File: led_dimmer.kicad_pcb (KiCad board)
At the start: 2 copper layers, 23.5 x 25.1 mm, 13 parts, among them P1 CONN_2, P2 CONN_2, Q1 MOSFET_N, U1 555

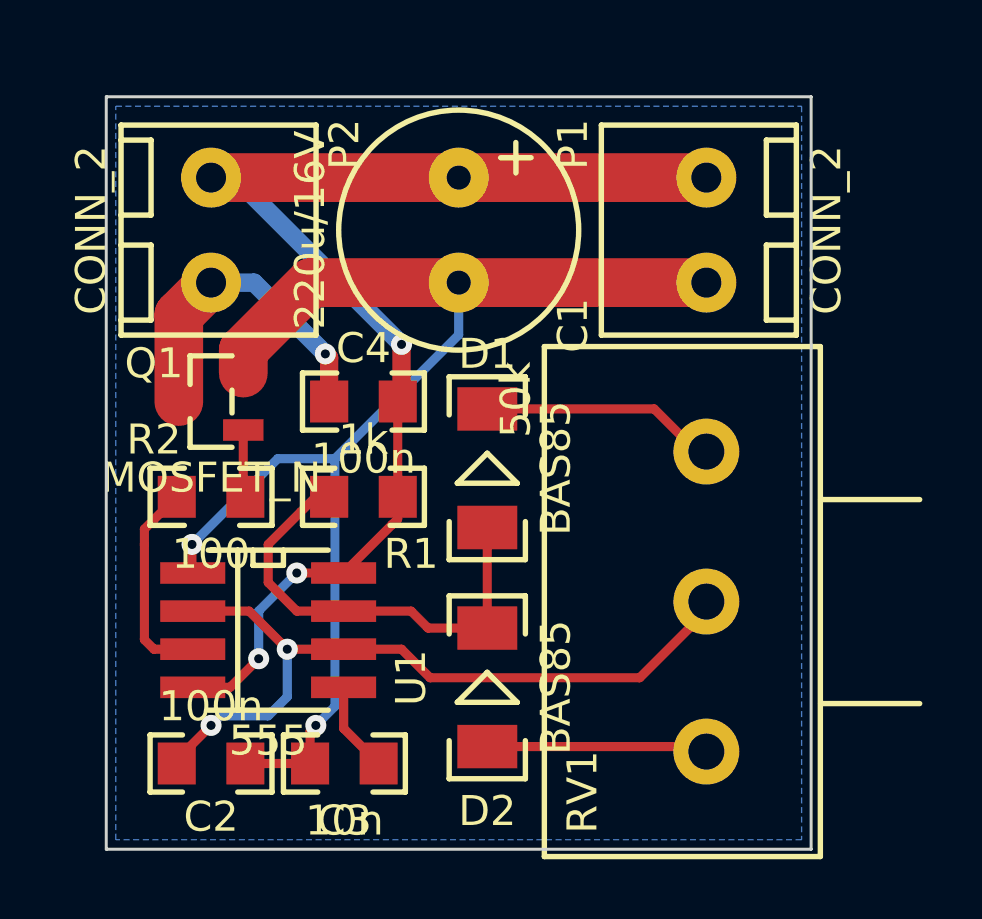
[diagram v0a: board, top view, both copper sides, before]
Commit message: larger vias, silk screen update
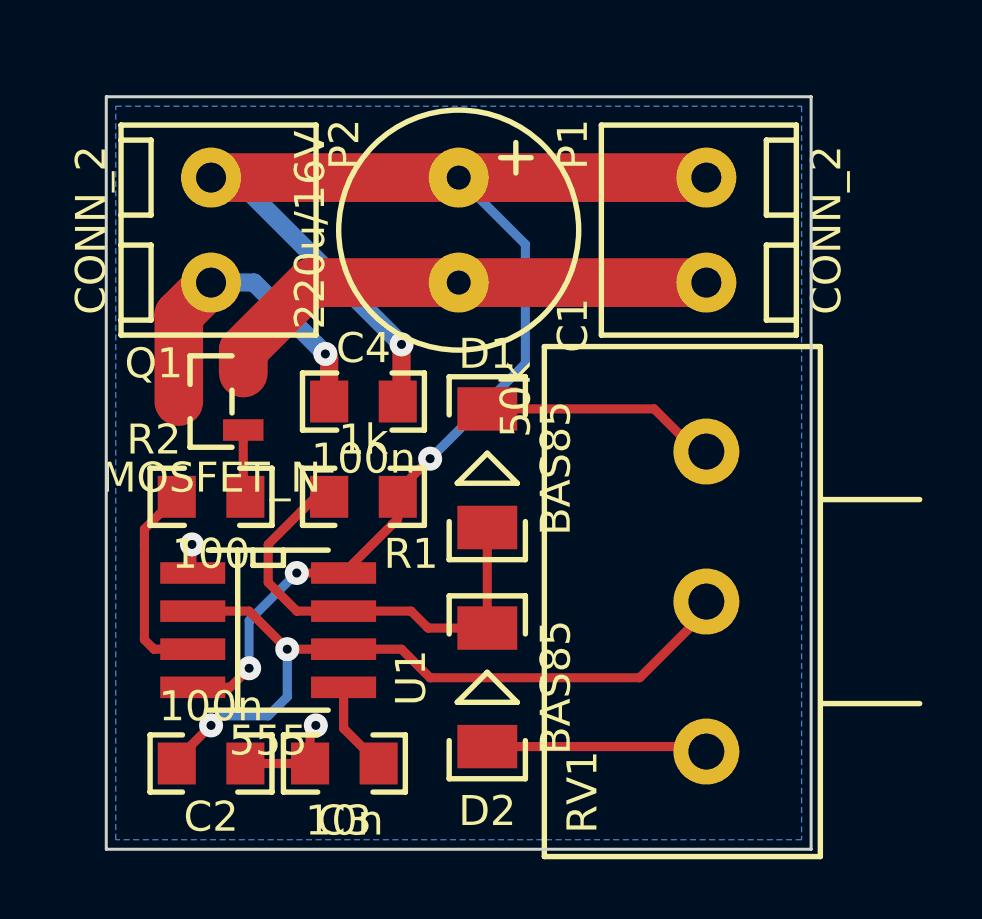
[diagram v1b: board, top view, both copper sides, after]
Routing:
- net GND: track 44.3 -> 21.8 mm
- net VCC: track 41.1 -> 51.3 mm, vias 3 -> 4
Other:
- net class Default: clearance 0.2794 -> 0.3048; via_dia 0.7 -> 0.8
- rule trace_clearance: 0.2794 -> 0.3048
- rule via_min_size: 0.7 -> 0.8
- board text added: "LED"
- board text added: "LED dimmer"
- board text added: "PWR"
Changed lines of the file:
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@@
     (links 24)
     (no_connects 0)
-    (area 148.912029 97.965 180.201401 124.121901)
+    (area 148.886629 97.965 180.226801 124.147301)
     (thickness 1.6)
-    (drawings 8)
+    (drawings 11)
     (tracks 80)
     (zones 0)
@@
     (18 B.Paste user)
     (19 F.Paste user)
-    (20 B.SilkS user)
+    (20 B.SilkS user hide)
     (21 F.SilkS user)
     (22 B.Mask user)
@@
     (user_trace_width 0.6096)
     (user_trace_width 1.6256)
-    (trace_clearance 0.2794)
+    (trace_clearance 0.3048)
     (zone_clearance 0.2794)
     (zone_45_only no)
@@
     (segment_width 0.2)
     (edge_width 0.1)
-    (via_size 0.7)
+    (via_size 0.8)
     (via_drill 0.3)
-    (via_min_size 0.7)
+    (via_min_size 0.8)
     (via_min_drill 0.3)
     (uvia_size 0.508)
@@
   (net 10 VCC)
   (net_class Default "This is the default net class."
-    (clearance 0.2794)
+    (clearance 0.3048)
     (trace_width 0.3048)
-    (via_dia 0.7)
+    (via_dia 0.8)
     (via_drill 0.3)
     (uvia_dia 0.508)
@@
     )
   )
+  (gr_text PWR (at 172.72 107.315) (layer B.SilkS)
+    (effects (font (size 1.5 1.5) (thickness 0.3)) (justify mirror))
+  )
+  (gr_text LED (at 156.21 107.315) (layer B.SilkS)
+    (effects (font (size 1.5 1.5) (thickness 0.3)) (justify mirror))
+  )
+  (gr_text "LED\ndimmer" (at 163.83 116.205 90) (layer B.SilkS)
+    (effects (font (size 2 2) (thickness 0.3)) (justify mirror))
+  )
   (gr_text - (at 169.545 104.4575) (layer B.SilkS)
     (effects (font (size 3 3) (thickness 0.6)) (justify mirror))
@@
   (gr_line (start 176.2125 98.425) (end 152.7175 98.425) (angle 90) (layer Edge.Cuts) (width 0.1))
   (gr_line (start 152.7175 123.5075) (end 176.2125 123.5075) (angle 90) (layer Edge.Cuts) (width 0.1))
+  (segment (start 164.465 104.62) (end 164.465 104.775) (width 0.3048) (layer B.Cu) (net 1))
   (segment (start 155.6 114.3) (end 155.575 114.275) (width 0.3048) (layer F.Cu) (net 1))
-  (segment (start 158.4325 110.49) (end 160.3375 110.49) (width 0.3048) (layer B.Cu) (net 1))
-  (segment (start 155.575 113.3475) (end 158.4325 110.49) (width 0.3048) (layer B.Cu) (net 1))
-  (via (at 155.575 113.3475) (size 0.7) (layers F.Cu B.Cu) (net 1))
   (segment (start 155.575 114.275) (end 155.575 113.3475) (width 0.3048) (layer F.Cu) (net 1))
-  (segment (start 160.3375 110.49) (end 164.465 106.3625) (width 0.3048) (layer B.Cu) (net 1))
+  (via (at 155.575 113.3475) (size 0.8) (layers F.Cu B.Cu) (net 1))
   (segment (start 159.512 119.5705) (end 159.7025 119.38) (width 0.3048) (layer F.Cu) (net 1))
-  (via (at 159.7025 119.38) (size 0.7) (layers F.Cu B.Cu) (net 1))
-  (segment (start 159.7025 119.38) (end 160.3375 118.745) (width 0.3048) (layer B.Cu) (net 1))
-  (segment (start 160.3375 118.745) (end 160.3375 110.49) (width 0.3048) (layer B.Cu) (net 1))
   (segment (start 159.512 120.65) (end 159.512 119.5705) (width 0.3048) (layer F.Cu) (net 1) (status 10))
-  (segment (start 164.465 106.3625) (end 164.465 104.62) (width 0.3048) (layer B.Cu) (net 1))
+  (via (at 159.7025 119.38) (size 0.8) (layers F.Cu B.Cu) (net 1))
   (segment (start 157.285 107.635) (end 157.285 106.875) (width 1.6256) (layer F.Cu) (net 1) (status 10))
   (segment (start 157.285 106.875) (end 159.54 104.62) (width 1.6256) (layer F.Cu) (net 1))
@@
   (segment (start 162.56 116.84) (end 163.5125 117.7925) (width 0.3048) (layer F.Cu) (net 2))
   (segment (start 155.067 120.65) (end 155.067 120.523) (width 0.3048) (layer F.Cu) (net 2) (status 30))
-  (via (at 158.75 116.84) (size 0.7) (layers F.Cu B.Cu) (net 2))
+  (via (at 158.75 116.84) (size 0.8) (layers F.Cu B.Cu) (net 2))
   (segment (start 158.75 118.4275) (end 158.75 116.84) (width 0.3048) (layer B.Cu) (net 2))
   (segment (start 158.115 119.0625) (end 158.75 118.4275) (width 0.3048) (layer B.Cu) (net 2))
   (segment (start 156.5275 119.0625) (end 158.115 119.0625) (width 0.3048) (layer B.Cu) (net 2))
   (segment (start 156.21 119.38) (end 156.5275 119.0625) (width 0.3048) (layer B.Cu) (net 2))
-  (via (at 156.21 119.38) (size 0.7) (layers F.Cu B.Cu) (net 2))
+  (via (at 156.21 119.38) (size 0.8) (layers F.Cu B.Cu) (net 2))
   (segment (start 155.067 120.523) (end 156.21 119.38) (width 0.3048) (layer F.Cu) (net 2) (status 10))
   (segment (start 160.63 116.84) (end 158.75 116.84) (width 0.3048) (layer F.Cu) (net 2) (status 10))
@@
   (segment (start 157.6425 104.62) (end 156.21 104.62) (width 0.6096) (layer B.Cu) (net 4) (status 20))
   (segment (start 160.02 106.9975) (end 157.6425 104.62) (width 0.6096) (layer B.Cu) (net 4))
-  (via (at 160.02 106.9975) (size 0.7) (layers F.Cu B.Cu) (net 4))
+  (via (at 160.02 106.9975) (size 0.8) (layers F.Cu B.Cu) (net 4))
   (segment (start 160.147 107.1245) (end 160.02 106.9975) (width 0.6096) (layer F.Cu) (net 4))
   (segment (start 155.135 108.585) (end 155.135 105.695) (width 1.6256) (layer F.Cu) (net 4) (status 10))
@@
   (segment (start 153.9875 116.5225) (end 154.305 116.84) (width 0.3048) (layer F.Cu) (net 9))
   (segment (start 153.9875 112.8395) (end 153.9875 113.3475) (width 0.3048) (layer F.Cu) (net 9))
-  (segment (start 162.433 108.585) (end 162.433 111.76) (width 0.3048) (layer F.Cu) (net 10))
+  (segment (start 162.433 111.76) (end 162.433 111.5695) (width 0.3048) (layer F.Cu) (net 10))
+  (segment (start 166.6875 103.3425) (end 164.465 101.12) (width 0.3048) (layer B.Cu) (net 10))
+  (segment (start 166.6875 107.315) (end 166.6875 103.3425) (width 0.3048) (layer B.Cu) (net 10))
+  (segment (start 163.5125 110.49) (end 166.6875 107.315) (width 0.3048) (layer B.Cu) (net 10))
+  (via (at 163.5125 110.49) (size 0.8) (layers F.Cu B.Cu) (net 10))
+  (segment (start 162.433 111.5695) (end 163.5125 110.49) (width 0.3048) (layer F.Cu) (net 10))
   (segment (start 162.433 111.76) (end 162.433 112.497) (width 0.3048) (layer F.Cu) (net 10))
   (segment (start 162.2425 112.6875) (end 160.63 114.3) (width 0.3048) (layer F.Cu) (net 10) (status 20))
@@
   (segment (start 160.63 114.3) (end 159.0675 114.3) (width 0.3048) (layer F.Cu) (net 10) (status 10))
   (segment (start 156.845 118.11) (end 155.6 118.11) (width 0.3048) (layer F.Cu) (net 10) (status 20))
-  (segment (start 157.7975 117.1575) (end 156.845 118.11) (width 0.3048) (layer F.Cu) (net 10))
-  (via (at 157.7975 117.1575) (size 0.7) (layers F.Cu B.Cu) (net 10))
-  (segment (start 157.7975 115.57) (end 157.7975 117.1575) (width 0.3048) (layer B.Cu) (net 10))
-  (segment (start 159.0675 114.3) (end 157.7975 115.57) (width 0.3048) (layer B.Cu) (net 10))
-  (via (at 159.0675 114.3) (size 0.7) (layers F.Cu B.Cu) (net 10))
+  (segment (start 157.48 117.475) (end 156.845 118.11) (width 0.3048) (layer F.Cu) (net 10))
+  (via (at 157.48 117.475) (size 0.8) (layers F.Cu B.Cu) (net 10))
+  (segment (start 157.48 115.8875) (end 157.48 117.475) (width 0.3048) (layer B.Cu) (net 10))
+  (segment (start 159.0675 114.3) (end 157.48 115.8875) (width 0.3048) (layer B.Cu) (net 10))
+  (via (at 159.0675 114.3) (size 0.8) (layers F.Cu B.Cu) (net 10))
   (segment (start 162.433 108.585) (end 162.56 108.458) (width 0.6096) (layer F.Cu) (net 10) (status 30))
   (segment (start 162.56 108.458) (end 162.56 106.68) (width 0.6096) (layer F.Cu) (net 10) (status 10))
   (segment (start 157 101.12) (end 156.21 101.12) (width 0.6096) (layer B.Cu) (net 10) (status 30))
   (segment (start 162.56 106.68) (end 157 101.12) (width 0.6096) (layer B.Cu) (net 10) (status 20))
-  (via (at 162.56 106.68) (size 0.7) (layers F.Cu B.Cu) (net 10))
+  (via (at 162.56 106.68) (size 0.8) (layers F.Cu B.Cu) (net 10))
   (segment (start 156.21 101.12) (end 164.465 101.12) (width 1.6256) (layer F.Cu) (net 10) (status 30))
   (segment (start 164.465 101.12) (end 172.72 101.12) (width 1.6256) (layer F.Cu) (net 10) (status 30))

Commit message: removed redundant vias
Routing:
- net Net-(C2-Pad2): track 25.2 -> 24.7 mm, vias 2 -> 0
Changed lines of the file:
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@@
     (thickness 1.6)
     (drawings 11)
-    (tracks 80)
+    (tracks 74)
     (zones 0)
     (modules 13)
@@
   (gr_line (start 176.2125 98.425) (end 152.7175 98.425) (angle 90) (layer Edge.Cuts) (width 0.1))
   (gr_line (start 152.7175 123.5075) (end 176.2125 123.5075) (angle 90) (layer Edge.Cuts) (width 0.1))
-  (segment (start 164.465 104.62) (end 164.465 104.775) (width 0.3048) (layer B.Cu) (net 1))
-  (segment (start 155.6 114.3) (end 155.575 114.275) (width 0.3048) (layer F.Cu) (net 1))
-  (segment (start 155.575 114.275) (end 155.575 113.3475) (width 0.3048) (layer F.Cu) (net 1))
+  (segment (start 164.465 104.62) (end 164.465 104.775) (width 0.3048) (layer B.Cu) (net 1) (status 30))
+  (segment (start 155.6 114.3) (end 155.575 114.275) (width 0.3048) (layer F.Cu) (net 1) (status 30))
+  (segment (start 155.575 114.275) (end 155.575 113.3475) (width 0.3048) (layer F.Cu) (net 1) (status 10))
   (via (at 155.575 113.3475) (size 0.8) (layers F.Cu B.Cu) (net 1))
   (segment (start 159.512 119.5705) (end 159.7025 119.38) (width 0.3048) (layer F.Cu) (net 1))
@@
   (segment (start 164.465 104.62) (end 172.72 104.62) (width 1.6256) (layer F.Cu) (net 1) (status 30))
   (segment (start 157.353 120.65) (end 159.512 120.65) (width 0.3048) (layer F.Cu) (net 1) (status 30))
-  (segment (start 160.63 116.84) (end 162.56 116.84) (width 0.3048) (layer F.Cu) (net 2))
-  (segment (start 170.4975 117.7925) (end 172.72 115.57) (width 0.3048) (layer F.Cu) (net 2))
+  (segment (start 158.75 116.84) (end 158.75 117.475) (width 0.3048) (layer F.Cu) (net 2))
+  (segment (start 155.067 120.523) (end 156.21 119.38) (width 0.3048) (layer F.Cu) (net 2) (status 10))
+  (segment (start 155.067 120.523) (end 155.067 120.65) (width 0.3048) (layer F.Cu) (net 2) (status 30))
+  (segment (start 156.845 119.38) (end 156.21 119.38) (width 0.3048) (layer F.Cu) (net 2))
+  (segment (start 158.75 117.475) (end 156.845 119.38) (width 0.3048) (layer F.Cu) (net 2))
+  (segment (start 160.63 116.84) (end 162.56 116.84) (width 0.3048) (layer F.Cu) (net 2) (status 10))
+  (segment (start 170.4975 117.7925) (end 172.72 115.57) (width 0.3048) (layer F.Cu) (net 2) (status 20))
   (segment (start 163.5125 117.7925) (end 170.4975 117.7925) (width 0.3048) (layer F.Cu) (net 2))
   (segment (start 162.56 116.84) (end 163.5125 117.7925) (width 0.3048) (layer F.Cu) (net 2))
-  (segment (start 155.067 120.65) (end 155.067 120.523) (width 0.3048) (layer F.Cu) (net 2) (status 30))
-  (via (at 158.75 116.84) (size 0.8) (layers F.Cu B.Cu) (net 2))
-  (segment (start 158.75 118.4275) (end 158.75 116.84) (width 0.3048) (layer B.Cu) (net 2))
-  (segment (start 158.115 119.0625) (end 158.75 118.4275) (width 0.3048) (layer B.Cu) (net 2))
-  (segment (start 156.5275 119.0625) (end 158.115 119.0625) (width 0.3048) (layer B.Cu) (net 2))
-  (segment (start 156.21 119.38) (end 156.5275 119.0625) (width 0.3048) (layer B.Cu) (net 2))
-  (via (at 156.21 119.38) (size 0.8) (layers F.Cu B.Cu) (net 2))
-  (segment (start 155.067 120.523) (end 156.21 119.38) (width 0.3048) (layer F.Cu) (net 2) (status 10))
   (segment (start 160.63 116.84) (end 158.75 116.84) (width 0.3048) (layer F.Cu) (net 2) (status 10))
   (segment (start 157.48 115.57) (end 155.6 115.57) (width 0.3048) (layer F.Cu) (net 2) (status 20))
@@
   (segment (start 155.135 108.585) (end 155.135 105.695) (width 1.6256) (layer F.Cu) (net 4) (status 10))
   (segment (start 155.135 105.695) (end 156.21 104.62) (width 1.6256) (layer F.Cu) (net 4) (status 20))
-  (segment (start 159.1945 112.268) (end 159.7025 111.76) (width 0.3048) (layer F.Cu) (net 5))
+  (segment (start 158.115 113.3475) (end 159.7025 111.76) (width 0.3048) (layer F.Cu) (net 5) (status 20))
   (segment (start 159.0675 115.57) (end 158.115 114.6175) (width 0.3048) (layer F.Cu) (net 5))
   (segment (start 158.115 114.6175) (end 158.115 113.3475) (width 0.3048) (layer F.Cu) (net 5))
-  (segment (start 158.115 113.3475) (end 159.1945 112.268) (width 0.3048) (layer F.Cu) (net 5))
   (segment (start 160.63 115.57) (end 159.0675 115.57) (width 0.3048) (layer F.Cu) (net 5) (status 10))
-  (segment (start 159.7025 111.76) (end 160.147 111.76) (width 0.3048) (layer F.Cu) (net 5))
-  (segment (start 165.4175 112.7825) (end 165.4175 116.135) (width 0.3048) (layer F.Cu) (net 5))
-  (segment (start 160.63 115.57) (end 162.8775 115.57) (width 0.3048) (layer F.Cu) (net 5))
-  (segment (start 163.4425 116.135) (end 165.4175 116.135) (width 0.3048) (layer F.Cu) (net 5))
+  (segment (start 159.7025 111.76) (end 160.147 111.76) (width 0.3048) (layer F.Cu) (net 5) (status 30))
+  (segment (start 165.4175 112.7825) (end 165.4175 116.135) (width 0.3048) (layer F.Cu) (net 5) (status 30))
+  (segment (start 160.63 115.57) (end 162.8775 115.57) (width 0.3048) (layer F.Cu) (net 5) (status 10))
+  (segment (start 163.4425 116.135) (end 165.4175 116.135) (width 0.3048) (layer F.Cu) (net 5) (status 20))
   (segment (start 162.8775 115.57) (end 163.4425 116.135) (width 0.3048) (layer F.Cu) (net 5))
-  (segment (start 165.4175 108.8325) (end 170.9825 108.8325) (width 0.3048) (layer F.Cu) (net 6))
-  (segment (start 170.9825 108.8325) (end 172.72 110.57) (width 0.3048) (layer F.Cu) (net 6))
-  (segment (start 165.4175 120.085) (end 172.235 120.085) (width 0.3048) (layer F.Cu) (net 7))
-  (segment (start 172.235 120.085) (end 172.72 120.57) (width 0.3048) (layer F.Cu) (net 7))
-  (segment (start 157.353 111.76) (end 157.285 111.692) (width 0.3048) (layer F.Cu) (net 8))
-  (segment (start 157.285 111.692) (end 157.285 109.535) (width 0.3048) (layer F.Cu) (net 8))
-  (segment (start 155.067 111.76) (end 153.9875 112.8395) (width 0.3048) (layer F.Cu) (net 9))
+  (segment (start 165.4175 108.8325) (end 170.9825 108.8325) (width 0.3048) (layer F.Cu) (net 6) (status 10))
+  (segment (start 170.9825 108.8325) (end 172.72 110.57) (width 0.3048) (layer F.Cu) (net 6) (status 20))
+  (segment (start 165.4175 120.085) (end 172.235 120.085) (width 0.3048) (layer F.Cu) (net 7) (status 30))
+  (segment (start 172.235 120.085) (end 172.72 120.57) (width 0.3048) (layer F.Cu) (net 7) (status 30))
+  (segment (start 157.353 111.76) (end 157.285 111.692) (width 0.3048) (layer F.Cu) (net 8) (status 30))
+  (segment (start 157.285 111.692) (end 157.285 109.535) (width 0.3048) (layer F.Cu) (net 8) (status 30))
+  (segment (start 155.067 111.76) (end 153.9875 112.8395) (width 0.3048) (layer F.Cu) (net 9) (status 10))
   (segment (start 154.305 116.84) (end 155.6 116.84) (width 0.3048) (layer F.Cu) (net 9) (status 20))
-  (segment (start 153.9875 113.3475) (end 153.9875 116.5225) (width 0.3048) (layer F.Cu) (net 9))
+  (segment (start 153.9875 112.8395) (end 153.9875 116.5225) (width 0.3048) (layer F.Cu) (net 9))
   (segment (start 153.9875 116.5225) (end 154.305 116.84) (width 0.3048) (layer F.Cu) (net 9))
-  (segment (start 153.9875 112.8395) (end 153.9875 113.3475) (width 0.3048) (layer F.Cu) (net 9))
-  (segment (start 162.433 111.76) (end 162.433 111.5695) (width 0.3048) (layer F.Cu) (net 10))
-  (segment (start 166.6875 103.3425) (end 164.465 101.12) (width 0.3048) (layer B.Cu) (net 10))
+  (segment (start 162.433 111.76) (end 162.433 111.5695) (width 0.3048) (layer F.Cu) (net 10) (status 30))
+  (segment (start 166.6875 103.3425) (end 164.465 101.12) (width 0.3048) (layer B.Cu) (net 10) (status 20))
   (segment (start 166.6875 107.315) (end 166.6875 103.3425) (width 0.3048) (layer B.Cu) (net 10))
   (segment (start 163.5125 110.49) (end 166.6875 107.315) (width 0.3048) (layer B.Cu) (net 10))
   (via (at 163.5125 110.49) (size 0.8) (layers F.Cu B.Cu) (net 10))
-  (segment (start 162.433 111.5695) (end 163.5125 110.49) (width 0.3048) (layer F.Cu) (net 10))
-  (segment (start 162.433 111.76) (end 162.433 112.497) (width 0.3048) (layer F.Cu) (net 10))
-  (segment (start 162.2425 112.6875) (end 160.63 114.3) (width 0.3048) (layer F.Cu) (net 10) (status 20))
-  (segment (start 162.433 112.497) (end 162.2425 112.6875) (width 0.3048) (layer F.Cu) (net 10))
+  (segment (start 162.433 111.5695) (end 163.5125 110.49) (width 0.3048) (layer F.Cu) (net 10) (status 10))
+  (segment (start 162.433 111.76) (end 162.433 112.497) (width 0.3048) (layer F.Cu) (net 10) (status 10))
+  (segment (start 162.433 112.497) (end 160.63 114.3) (width 0.3048) (layer F.Cu) (net 10) (status 20))
   (segment (start 160.63 114.3) (end 159.0675 114.3) (width 0.3048) (layer F.Cu) (net 10) (status 10))
   (segment (start 156.845 118.11) (end 155.6 118.11) (width 0.3048) (layer F.Cu) (net 10) (status 20))
